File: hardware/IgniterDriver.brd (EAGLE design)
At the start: 160 x 100 mm, 22 parts, among them IC1 ATMEGA48/88/168-AU, Q1 FDD4141TO252, Q2 IRLML5203, Q4 16MHz, U2 MCP25625-E/SS

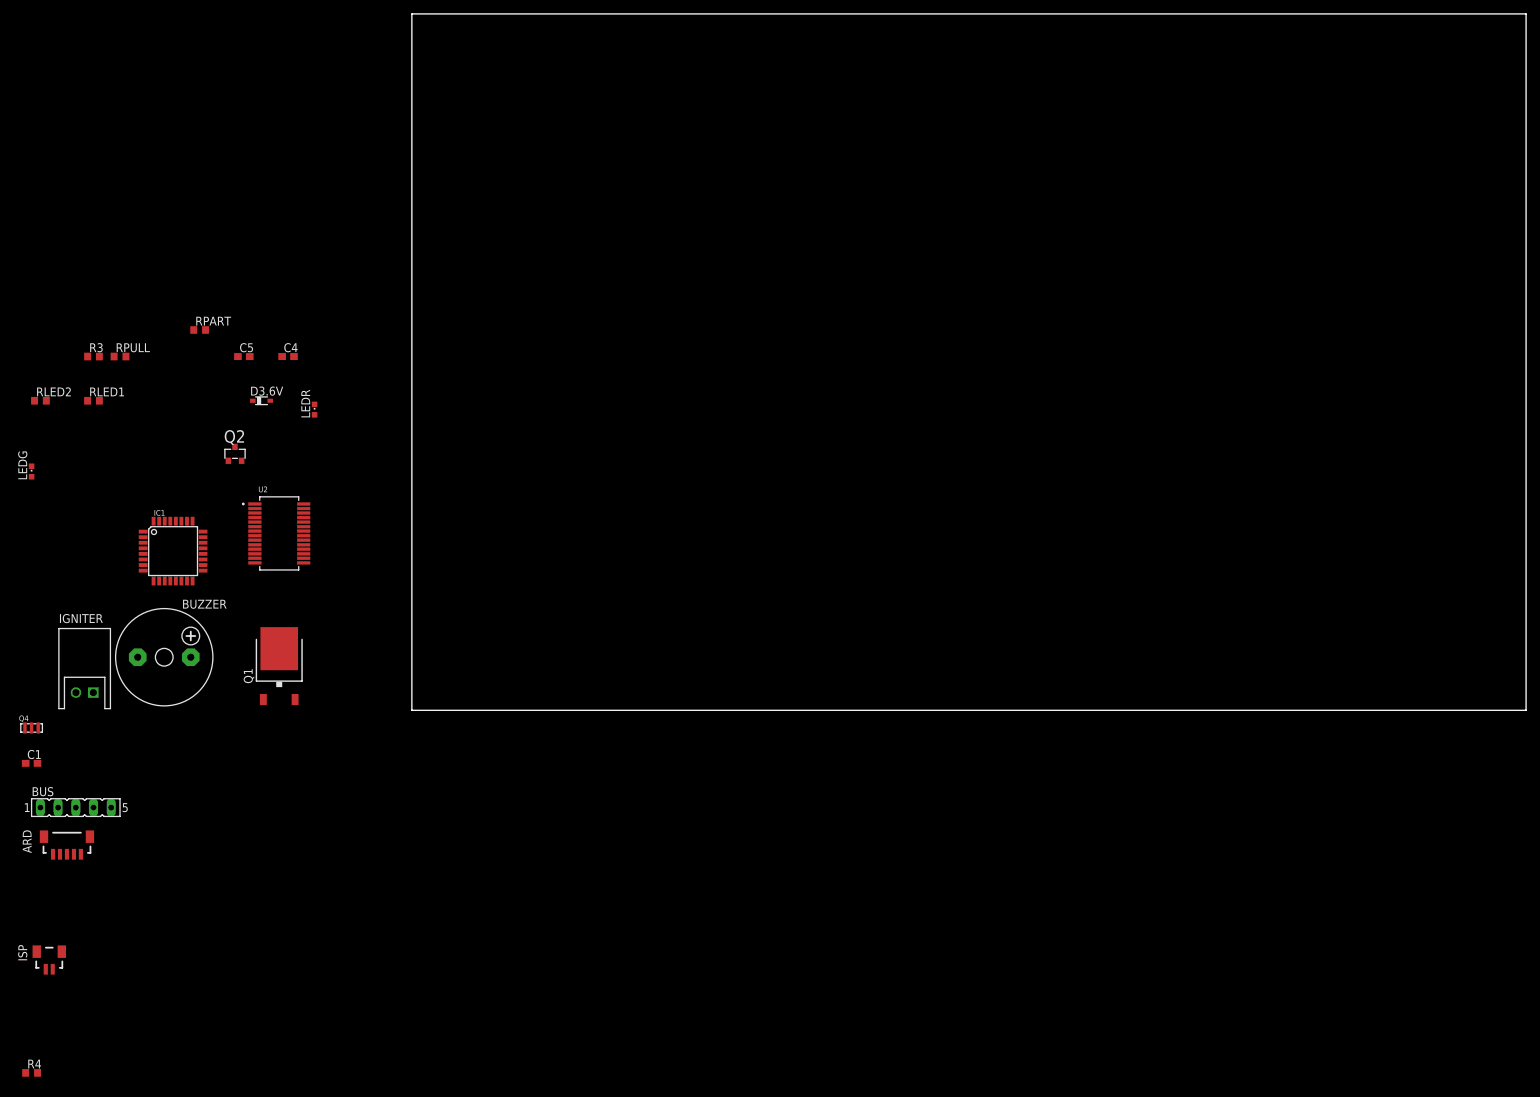
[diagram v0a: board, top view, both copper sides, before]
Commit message: Add igniter driver board
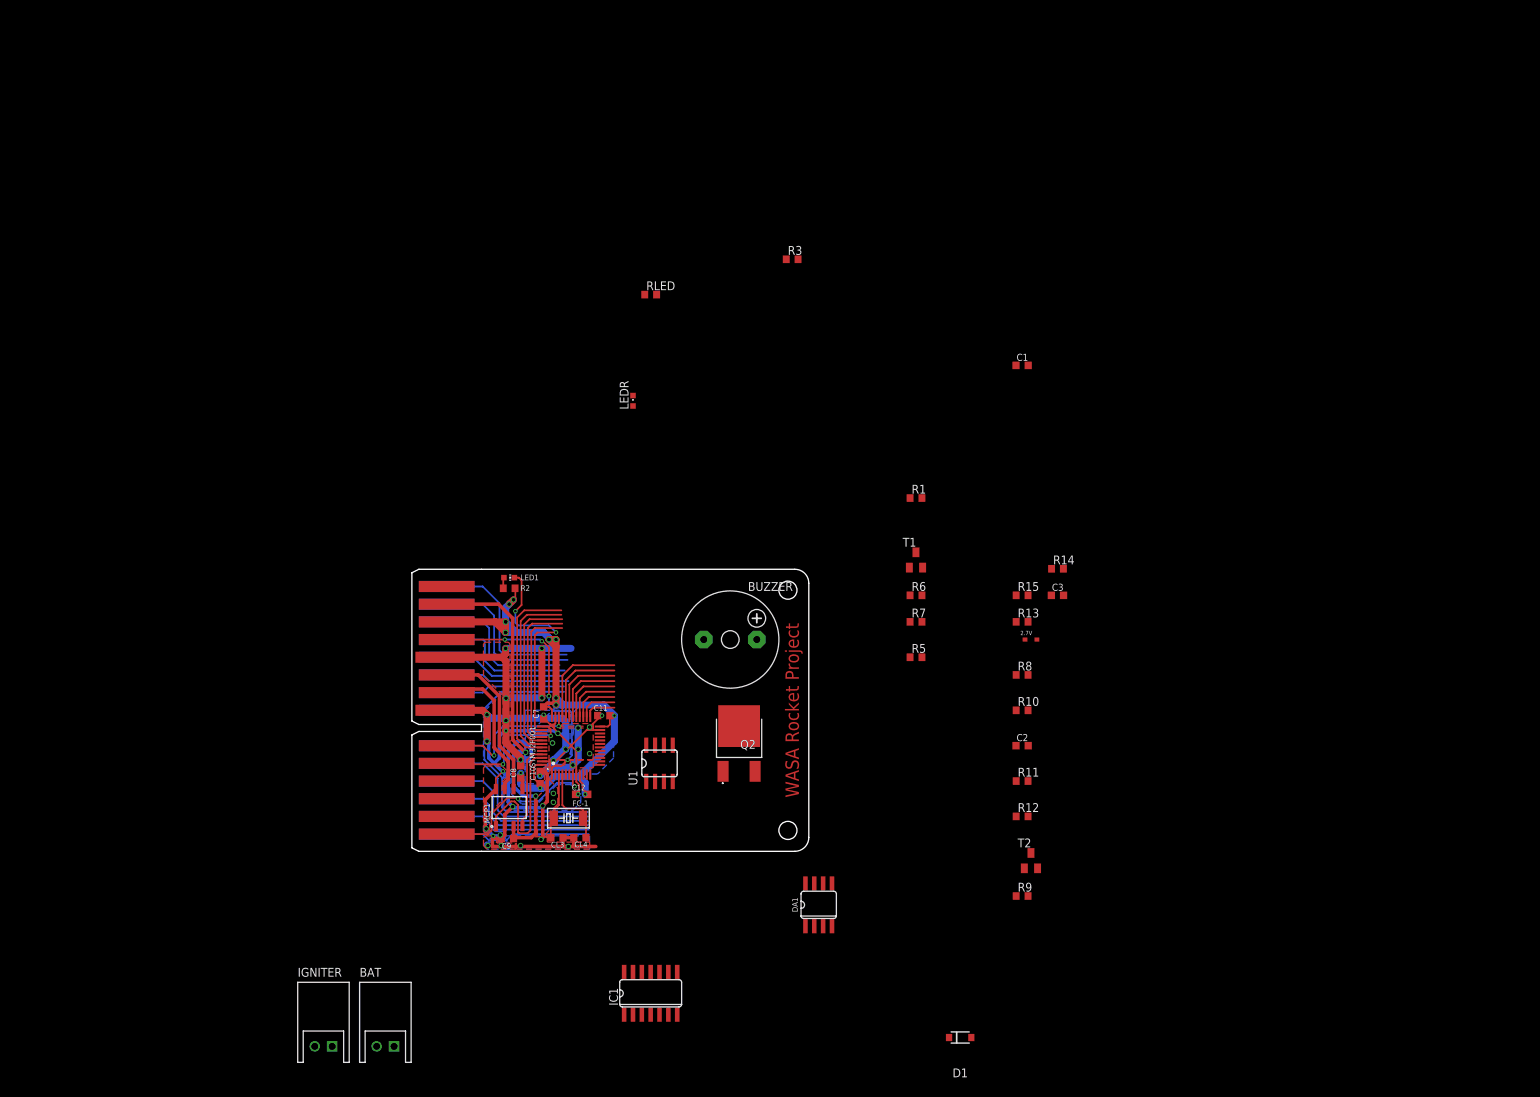
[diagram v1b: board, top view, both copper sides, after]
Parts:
- removed ARD: BM05B-SRSS-TB, con-jst2:BM05B-SRSS-TB
- removed BUS: (no value), con-lsta:FE05-1
- removed C4, C5: 0.1μF, rcl:C0603
- removed D3.6V: BAT60J, diode:SOD323_ST
- removed ISP: BM02B-SRSS-TB, con-jst2:BM02B-SRSS-TB
- removed LEDG: (no value), led:CHIPLED_0603
- removed Q1: FDD4141TO252, transistor-fet:TO252
- removed Q4: 16MHz, m-pad-2.1:RESONATOR_MURATA2
- removed R4: 1K, rcl:R0603
- removed RLED1, RLED2: 470, rcl:R0603
- removed RPART: (no value), rcl:R0603
- removed RPULL: 10k, rcl:R0603
- removed U2: MCP25625-E/SS, mcp25625-E_SS:SOP65P780X200-28N
- added 2.7V: BZX584C2V7, diodes:BZX584C
- added BAT: (no value), con-jst-xh:S2B-XH-A
- added C10, C11, C12, C7, C8, C9: (no value), rcl:C0603K
- added C2, C3: 1nF, rcl:C0603K
- added CL3, CL4: 15pF, rcl:C0603K
- added D1: RB160M-30TR, RB160M-30TR:SODFL3516X90N
- added DA1: NJM2904M, ic-jrc:SO-8
- added FC-1: 32.768kHz, crystal':FC-255
- added LED1: (no value), led:CHIP-LED0603
- added MCP1: MCP2562-E/SN, mcp2562-E_SN:SOIC127P600X175-8N
- added R1, R7: 10k, rcl:R0603
- added R10, R11, R12, R13, R14, R5, R6, R9: 1k, rcl:R0603
- added R15: 100k, rcl:R0603
- added R2: (no value), rcl:R0603
- added R8: 100, rcl:R0603
- added RLED: 470, rcl:R0603
- added STM32F001: STM32F072-LQFP48, stm32f0:LQFP48
- added T1, T2: (no value), transistor:SOT23-EBC
- added U$2: EDGE30, bus:EDGE30
- added U1: ACS711ELCTR-12AB-T, allegro:SOIC8
- C1: value 0.1μF -> 0.1µF; device rcl:C0603 -> rcl:C0603K
- IC1: value ATMEGA48/88/168-AU -> 4066D; device atmega8:TQFP32-08 -> 40xx:SO14
- Q2: value IRLML5203 -> TJ8S06M3L(T6L1,NQ); device transistor-power:MICRO3 -> TJ8S06M3L(T6L1_NQ):TJ8S06M3LT6L1NQ
- moved C1 153.3 mm to (87.6, 49.5)
- moved R3 101.3 mm to (54.6, 64.8)
- moved IC1 93.5 mm to (34.3, -40.6)
- moved Q2 81.8 mm to (47.0, -1.27)
- moved BUZZER 81.3 mm to (45.7, 10.2)
- moved IGNITER 61.3 mm to (-12.7, -48.3)
- moved LEDR 45.7 mm to (31.8, 44.5)
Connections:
- removed net MISO: IC1.16, ISP.1, U2.16
- removed net MOSI: IC1.15, ISP.2, U2.15
- removed net N$10: U2.20, U2.24
- removed net N$14: IC1.27, R3.1
- removed net N$18: IC1.32, U2.13
- removed net N$26: IC1.14, U2.17
- removed net N$27: Q4.1, U2.8
- removed net N$28: Q4.3, U2.9
- removed net N$29: IC1.13, U2.5
- removed net N$3: D3.6V.C, Q2.3, R4.1, RPART.1
- removed net N$30: IC1.11, U2.18
- removed net N$4: IC1.25, Q2.1
- removed net N$5: LEDR.A, RLED1.2
- removed net RX: ARD.3, IC1.30
- removed net TX: ARD.4, IC1.31
- removed net ~RESET: ARD.2, IC1.29
- new net BAT+: BAT.1, BUZZER.-, Q2.2, R1.2, R3.1
- new net BUZZER: R9.1, STM32F001.29
- new net CANH1: MCP1.7, U$2.7
- new net CANL1: MCP1.6, U$2.6
- new net CAN_RX: MCP1.4, STM32F001.45
- new net CAN_TX: MCP1.1, STM32F001.46
- new net CIG: DA1.7, R11.2, STM32F001.11
- new net CIG': C2.1, DA1.5, R12.2
- new net I2C1_SCK: STM32F001.43
- new net I2C1_SCL: STM32F001.42
- new net IG+': Q2.3, R13.1, R8.2, U1.1, U1.2
- new net IGNITE: R6.1, STM32F001.30
- new net N$15: R9.2, T2.B
- new net N$17: 2.7V.C, C3.1, DA1.3, R13.2
- new net N$46: U$2.30
- new net N$47: U$2.29
- new net N$48: U$2.28
- new net N$49: U$2.27
- new net N$50: U$2.26
- new net N$51: U$2.25
- new net N$52: U$2.23
- new net N$53: U$2.22
- new net N$54: U$2.21
- new net N$55: U$2.20
- new net N$56: U$2.19
- new net N$57: U$2.18
- new net N$60: STM32F001.12
- new net N$61: STM32F001.13
- new net N$62: STM32F001.14
- new net N$63: STM32F001.15
- new net N$64: STM32F001.16
- new net N$65: STM32F001.17
- new net N$67: STM32F001.32
- new net N$68: STM32F001.33
- new net N$69: STM32F001.18
- new net N$70: STM32F001.19
- new net N$71: STM32F001.20
- new net N$72: STM32F001.21
- new net N$73: STM32F001.22
- new net N$74: STM32F001.25
- new net N$75: STM32F001.26
- new net N$76: STM32F001.27
- new net N$77: STM32F001.28
- new net N$78: CL4.2, FC-1.1, STM32F001.4
- new net N$79: CL3.2, FC-1.2, STM32F001.3
- new net N$80: LED1.C, STM32F001.38
- new net N$81: U$2.16
- new net N$82: U$2.17
- new net N$83: LED1.A, R2.2
- new net NRST1: STM32F001.7, U$2.15
- new net SPI1_MISO: STM32F001.40
- new net SPI1_MOSI: STM32F001.41
- new net SPI1_SCK: STM32F001.39
- new net SWCLK1: STM32F001.37, U$2.11
- new net SWDIO1: STM32F001.34, U$2.10
- new net TEST: D1.2, STM32F001.31
- new net VBAT: STM32F001.1, U$2.4
- new net VIG: DA1.1, R15.2, STM32F001.10
- new net VSS: IC1.7
- net GND: now also 2.7V.A, BAT.2, C10.2, C11.2, C12.2, C2.2, C3.2, C7.2, C8.2, C9.2, CL3.1, CL4.1, DA1.4, MCP1.2, MCP1.8, R10.1, R14.1, R7.1, STM32F001.23, STM32F001.35, STM32F001.47, STM32F001.8, T1.E, T2.E, U$2.5, U$2.8, U1.5; no longer ARD.5, BUS.3, BUZZER.-, C4.2, C5.2, D3.6V.A, IC1.21, IC1.3, IC1.5, LEDG.C, Q4.2, RPULL.2, U2.10, U2.26
- net IG+: now also U1.3, U1.4; no longer Q1.3, RPART.2
- net N$1: now also Q2.1, R1.1, R5.1; no longer IC1.17, U2.14
- net N$11: now also DA1.2, R14.2, R15.1; no longer U2.21, U2.28
- net N$12: now also DA1.6, R10.2, R11.1; no longer IC1.26, RLED2.1
- net N$13: now also LEDR.A, RLED.2; no longer LEDG.A, RLED2.2
- net N$2: now also R5.2, T1.C; no longer IC1.23, R4.2
- net N$6: now also R6.2, R7.2, RLED.1, T1.B; no longer IC1.24, Q1.1, RLED1.1, RPULL.1
- net N$7: now also D1.1, R8.1; no longer BUS.5, U2.3
- net N$8: now also T2.C
- net N$9: now also R12.1, U1.7; no longer BUS.4, U2.4
- net VCC: now also C9.1, MCP1.3, U$2.2; no longer BUS.1, C1.1, U2.27
- net VDD: now also C1.1, C10.1, C11.1, C12.1, C7.1, C8.1, DA1.8, IC1.14, MCP1.5, R2.1, STM32F001.24, STM32F001.36, STM32F001.48, STM32F001.9, U$2.3, U1.8; no longer ARD.1, BUS.2, C4.1, C5.1, IC1.4, IC1.6, Q2.2, U2.1, U2.19
- net VPP: now also U$2.1; no longer Q1.2
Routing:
- net GND: track 0.00 -> 217.6 mm, vias 0 -> 35
- net VDD: track 0.00 -> 96.7 mm, vias 0 -> 12
- net VCC: track 0.00 -> 51.1 mm, vias 0 -> 2
- net VBAT: track 0.00 -> 38.0 mm, vias 0 -> 4
- net N$80: track 0.00 -> 31.9 mm, vias 0 -> 2
- net I2C1_SCK: track 0.00 -> 28.3 mm
- net N$51: track 0.00 -> 27.8 mm
- net I2C1_SCL: track 0.00 -> 26.3 mm
- net N$50: track 0.00 -> 26.1 mm
- net NRST1: track 0.00 -> 25.3 mm, vias 0 -> 2
- net N$81: track 0.00 -> 25.2 mm
- net N$49: track 0.00 -> 24.6 mm
- net SPI1_MOSI: track 0.00 -> 24.4 mm
- net N$82: track 0.00 -> 23.8 mm
- net CAN_TX: track 0.00 -> 23.3 mm
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- added copper zone on layer 1, net GND
- added copper zone on layer 16, net GND
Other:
- board size 160 x 100 mm -> 47 x 40.5 mm
- board text added: "WASA Rocket Project"

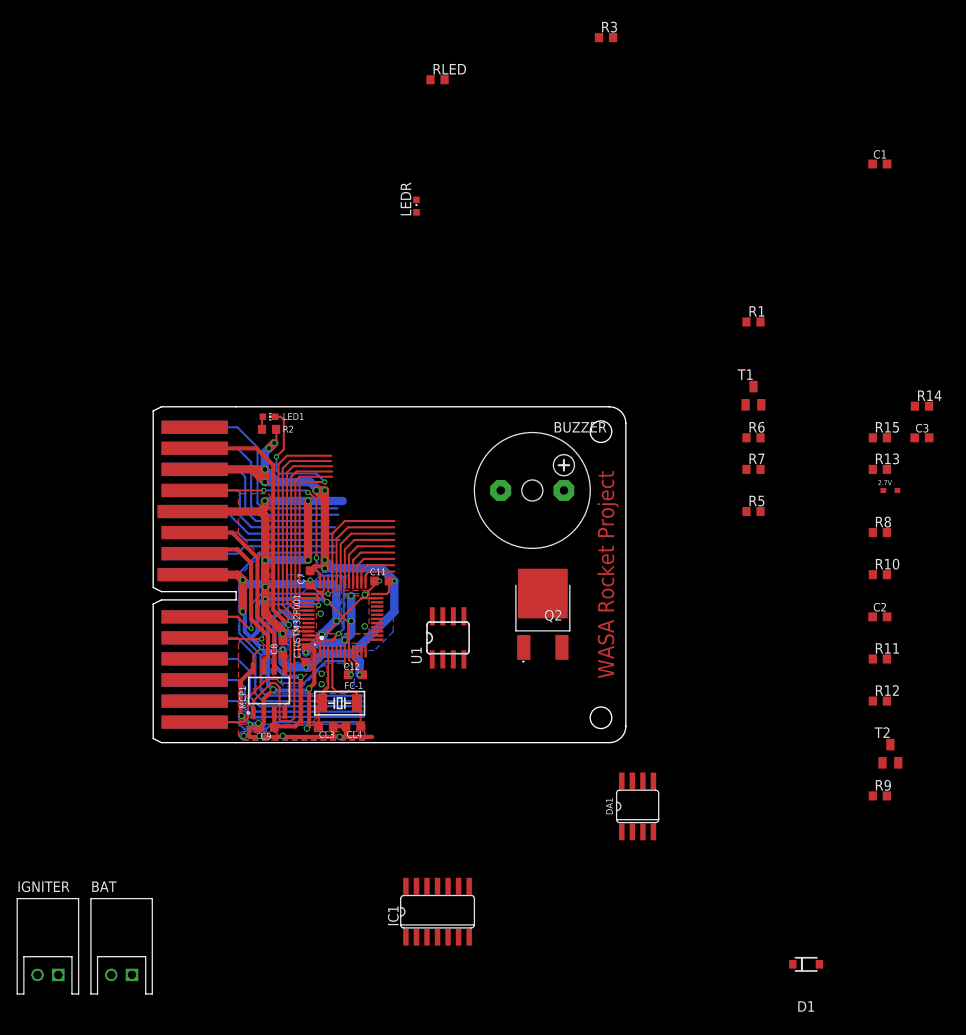
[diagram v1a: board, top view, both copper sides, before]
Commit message: Layout igniter driver board
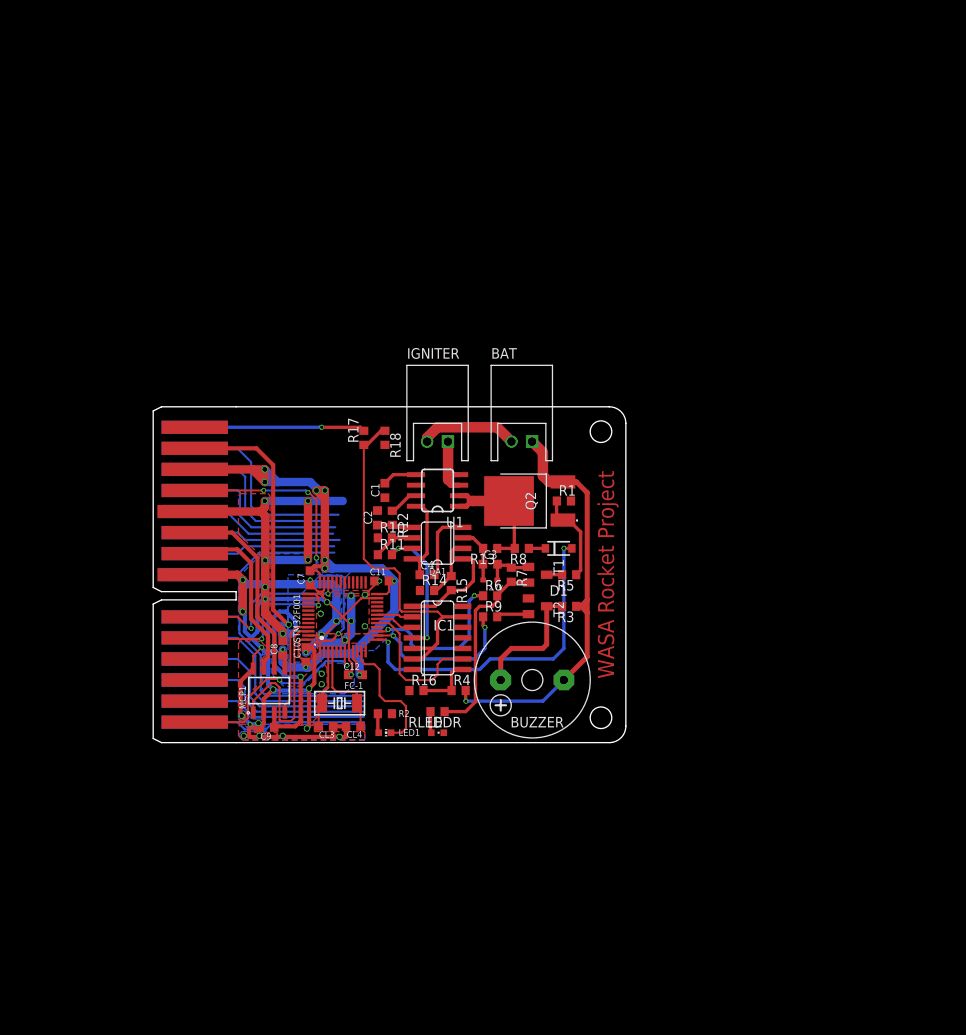
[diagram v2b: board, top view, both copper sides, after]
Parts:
- added C4: 0.1µF, rcl:C0603K
- added R16, R17: 1k, rcl:R0603
- added R18, R4: 10k, rcl:R0603
- moved BAT 80.4 mm to (44.5, 16.0)
- moved IGNITER 79.6 mm to (34.3, 16.0)
- moved RLED 76.2 mm to (34.3, -16.5), turned to 180 degrees
- moved C1 71.5 mm to (27.9, 10.2), turned to 90 degrees
- moved R3 68.7 mm to (50.2, -3.81), turned to 180 degrees
- moved R14 63.7 mm to (33.0, -1.91)
- moved LEDR 63.6 mm to (34.3, -19.1), turned to 270 degrees
- moved R12 62.8 mm to (28.8, 6.86), turned to 270 degrees
- moved C2 61.7 mm to (27.1, 6.86), turned to 90 degrees
- moved R11 61.0 mm to (27.9, 2.41)
- moved R10 59.9 mm to (27.9, 4.45)
- moved D1 58.4 mm to (48.9, 3.17)
- moved R15 54.6 mm to (35.9, -1.02), turned to 270 degrees
- moved C3 54.3 mm to (40.6, 1.27)
- moved R9 51.7 mm to (40.6, -5.08)
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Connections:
- net N$17 renamed VVIG
- net N$9 renamed VOUT
- removed net I2C1_SCK: STM32F001.43
- removed net I2C1_SCL: STM32F001.42
- removed net N$60: STM32F001.12
- removed net N$61: STM32F001.13
- removed net N$62: STM32F001.14
- removed net N$63: STM32F001.15
- removed net N$65: STM32F001.17
- removed net N$67: STM32F001.32
- removed net N$68: STM32F001.33
- removed net N$69: STM32F001.18
- removed net N$70: STM32F001.19
- removed net N$72: STM32F001.21
- removed net N$73: STM32F001.22
- removed net N$74: STM32F001.25
- removed net N$75: STM32F001.26
- removed net N$76: STM32F001.27
- removed net N$77: STM32F001.28
- removed net SPI1_MISO: STM32F001.40
- removed net SPI1_MOSI: STM32F001.41
- removed net SPI1_SCK: STM32F001.39
- new net !HIL!: IC1.13, IC1.5, IC1.6, R17.1, R18.1
- new net VBAT+: IC1.9, STM32F001.17
- new net VBAT+': IC1.8, R16.2, R4.1
- new net VCIG: C2.1, DA1.5, R12.2
- new net VIG': DA1.1, IC1.1, R15.2
- net BAT+: now also Q2.3, R4.2; no longer Q2.2
- net BUZZER: now also STM32F001.14; no longer STM32F001.29
- net CIG: now also IC1.3, STM32F001.18; no longer DA1.7, R11.2, STM32F001.11
- net CIG': now also DA1.7, IC1.4, R11.2; no longer C2.1, DA1.5, R12.2
- net GND: now also C4.2, R16.1
- net IG+': now also Q2.2; no longer Q2.3
- net IGNITE: now also STM32F001.15; no longer STM32F001.30
- net N$80: now also STM32F001.11; no longer STM32F001.38
- net N$81: now also R17.2
- net TEST: now also STM32F001.13; no longer STM32F001.31
- net VDD: now also C4.1, R18.2
- net VIG: now also IC1.2, STM32F001.19; no longer DA1.1, R15.2, STM32F001.10
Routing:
- net BAT+: track 0.00 -> 52.2 mm, vias 0 -> 1
- net !HIL!: track 0.00 -> 44.1 mm
- net I2C1_SCK: track 28.3 -> 0.00 mm
- net TEST: track 11.6 -> 39.5 mm, vias 0 -> 2
- net GND: track 217.6 -> 244.9 mm
- net I2C1_SCL: track 26.3 -> 0.00 mm
- net SPI1_MOSI: track 24.4 -> 0.00 mm
- net N$6: track 0.00 -> 23.5 mm
- net SPI1_MISO: track 22.5 -> 0.00 mm
- net SPI1_SCK: track 20.5 -> 0.00 mm
- net VBAT+: track 0.00 -> 17.8 mm
- net CIG': track 0.00 -> 17.7 mm, vias 0 -> 2
- net N$80: track 31.9 -> 15.3 mm, vias 2 -> 0
- net IG+': track 0.00 -> 16.2 mm
- net N$8: track 0.00 -> 15.3 mm
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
